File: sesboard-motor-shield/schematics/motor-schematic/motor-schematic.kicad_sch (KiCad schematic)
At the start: 0 parts

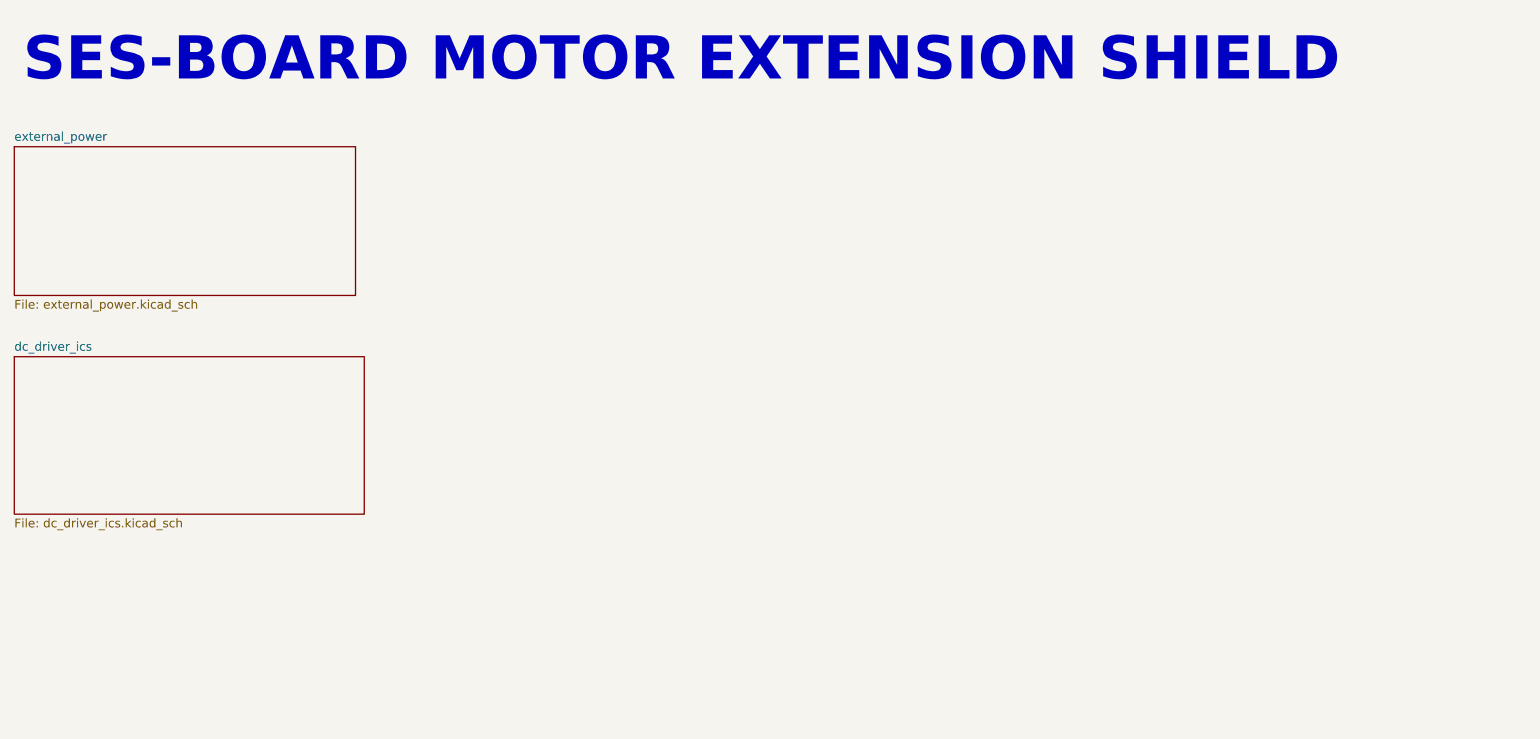
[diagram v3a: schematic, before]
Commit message: added global labels for motor drivers
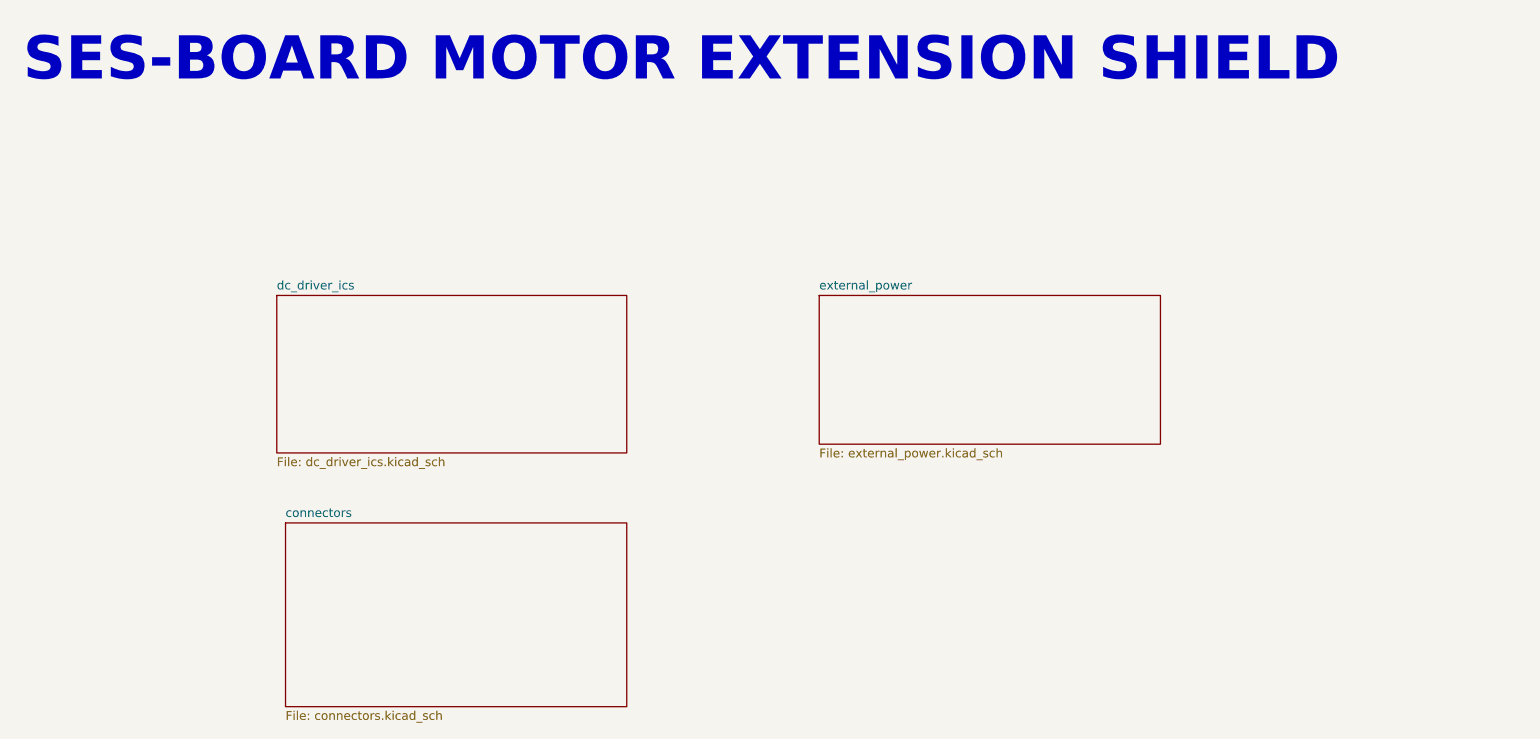
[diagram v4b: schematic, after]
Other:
- added sheet connectors (connectors.kicad_sch)
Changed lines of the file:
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@@
     (effects (font (size 6.27 6.27) (thickness 1.254) bold) (justify left bottom))
   )
-  (sheet (at 50.8 48.26) (size 49.53 21.59) (fields_autoplaced)
+  (sheet (at 90.17 102.87) (size 49.53 26.67) (fields_autoplaced)
     (stroke (width 0.1524) (type solid) (color 0 0 0 0))
     (fill (color 0 0 0 0.0000))
-    (property "Sheet name" "external_power" (id 0) (at 50.8 47.5484 0)
+    (property "Sheet name" "connectors" (id 0) (at 90.17 102.1584 0)
       (effects (font (size 1.27 1.27)) (justify left bottom))
     )
-    (property "Sheet file" "external_power.kicad_sch" (id 1) (at 50.8 70.4346 0)
+    (property "Sheet file" "connectors.kicad_sch" (id 1) (at 90.17 130.1246 0)
       (effects (font (size 1.27 1.27)) (justify left top))
     )
   )
-  (sheet (at 50.8 78.74) (size 50.8 22.86) (fields_autoplaced)
+  (sheet (at 167.64 69.85) (size 49.53 21.59) (fields_autoplaced)
     (stroke (width 0.1524) (type solid) (color 0 0 0 0))
     (fill (color 0 0 0 0.0000))
-    (property "Sheet name" "dc_driver_ics" (id 0) (at 50.8 78.0284 0)
+    (property "Sheet name" "external_power" (id 0) (at 167.64 69.1384 0)
       (effects (font (size 1.27 1.27)) (justify left bottom))
     )
-    (property "Sheet file" "dc_driver_ics.kicad_sch" (id 1) (at 50.8 102.1846 0)
+    (property "Sheet file" "external_power.kicad_sch" (id 1) (at 167.64 92.0246 0)
+      (effects (font (size 1.27 1.27)) (justify left top))
+    )
+  )
+  (sheet (at 88.9 69.85) (size 50.8 22.86) (fields_autoplaced)
+    (stroke (width 0.1524) (type solid) (color 0 0 0 0))
+    (fill (color 0 0 0 0.0000))
+    (property "Sheet name" "dc_driver_ics" (id 0) (at 88.9 69.1384 0)
+      (effects (font (size 1.27 1.27)) (justify left bottom))
+    )
+    (property "Sheet file" "dc_driver_ics.kicad_sch" (id 1) (at 88.9 93.2946 0)
       (effects (font (size 1.27 1.27)) (justify left top))
     )
@@
     (path "/93d2313f-0919-4c6f-b07d-ab630442d056" (page "2"))
     (path "/eeff06ce-5dd6-48ad-98cf-4489d7624b9c" (page "3"))
+    (path "/14cc8e54-6739-4c6f-a4bf-829f53e763f8" (page "4"))
   )
   (symbol_instances
@@
       (reference "#PWR025") (unit 1) (value "+5V") (footprint "")
     )
+    (path "/eeff06ce-5dd6-48ad-98cf-4489d7624b9c/d870bfca-195d-40b5-a5d5-c054209f3ecc"
+      (reference "#PWR?") (unit 1) (value "GND") (footprint "")
+    )
+    (path "/eeff06ce-5dd6-48ad-98cf-4489d7624b9c/e7b0b387-3fb1-41d8-b6b4-c4be9590eed9"
+      (reference "#PWR?") (unit 1) (value "GND") (footprint "")
+    )
     (path "/93d2313f-0919-4c6f-b07d-ab630442d056/d9ead9ee-c345-4017-a86b-e222369cda3f"
-      (reference "C1") (unit 1) (value "C") (footprint "")
+      (reference "C1") (unit 1) (value "C") (footprint "Capacitor_SMD:C_0603_1608Metric")
     )
     (path "/93d2313f-0919-4c6f-b07d-ab630442d056/5275729a-412a-4aea-939f-ed3f5e37f264"
-      (reference "C2") (unit 1) (value "10uF") (footprint "")
+      (reference "C2") (unit 1) (value "10uF") (footprint "Capacitor_SMD:C_0603_1608Metric")
     )
     (path "/93d2313f-0919-4c6f-b07d-ab630442d056/af78cc8e-1c8a-4ab5-9be6-d00d9f3661a8"
-      (reference "C3") (unit 1) (value "100nF") (footprint "")
+      (reference "C3") (unit 1) (value "100nF") (footprint "Capacitor_SMD:C_0603_1608Metric")
     )
     (path "/93d2313f-0919-4c6f-b07d-ab630442d056/2228ccfd-64fa-4f80-9e97-c17cd073ed77"
-      (reference "C4") (unit 1) (value "10uF") (footprint "")
+      (reference "C4") (unit 1) (value "10uF") (footprint "Capacitor_SMD:C_0603_1608Metric")
     )
     (path "/93d2313f-0919-4c6f-b07d-ab630442d056/22b8a583-4c69-4445-818a-792fb8c64310"
-      (reference "C5") (unit 1) (value "100nF") (footprint "")
+      (reference "C5") (unit 1) (value "100nF") (footprint "Capacitor_SMD:C_0603_1608Metric_Pad1.08x0.95mm_HandSolder")
     )
     (path "/93d2313f-0919-4c6f-b07d-ab630442d056/001a0253-6ecf-4292-a1f7-0f48edbbd35b"
-      (reference "D1") (unit 1) (value "GREEN_LED") (footprint "")
+      (reference "D1") (unit 1) (value "GREEN_LED") (footprint "LED_SMD:LED_0603_1608Metric")
     )
     (path "/93d2313f-0919-4c6f-b07d-ab630442d056/4f9418ba-9c6a-4f02-80b5-4d8b68173369"
-      (reference "J1") (unit 1) (value "Barrel_Jack") (footprint "")
+      (reference "J1") (unit 1) (value "Barrel_Jack") (footprint "Connector_BarrelJack:BarrelJack_Horizontal")
     )
     (path "/eeff06ce-5dd6-48ad-98cf-4489d7624b9c/c4453281-59ee-47d3-bd52-06aeb5935aac"
-      (reference "J2") (unit 1) (value "EXTERNAL_MOTOR_POWER") (footprint "")
+      (reference "J2") (unit 1) (value "EXTERNAL_MOTOR_POWER") (footprint "TerminalBlock_Phoenix:TerminalBlock_Phoenix_MKDS-1,5-2_1x02_P5.00mm_Horizontal")
     )
-    (path "/eeff06ce-5dd6-48ad-98cf-4489d7624b9c/d5013ac0-e1ec-465d-8ee5-8ced61108e8e"
-      (reference "J3") (unit 1) (value "MOTOR_C_OUT") (footprint "")
+    (path "/14cc8e54-6739-4c6f-a4bf-829f53e763f8/44d56e02-6f8b-4dba-a8f7-8cd6249ad3f6"
+      (reference "J3") (unit 1) (value "SESBOARD_1") (footprint "Connector_PinHeader_2.54mm:PinHeader_1x20_P2.54mm_Vertical")
     )
-    (path "/eeff06ce-5dd6-48ad-98cf-4489d7624b9c/bf4cd4e1-012f-42b7-8c27-76a7b81a4f28"
-      (reference "J4") (unit 1) (value "MOTOR_D_OUT") (footprint "")
+    (path "/14cc8e54-6739-4c6f-a4bf-829f53e763f8/19ccde18-a5b4-47c7-a5b9-970f62526c41"
+      (reference "J4") (unit 1) (value "SESBOARD_2") (footprint "Connector_PinHeader_2.54mm:PinHeader_1x20_P2.54mm_Vertical")
     )
-    (path "/eeff06ce-5dd6-48ad-98cf-4489d7624b9c/97dd2f34-1862-4f35-913e-e493c6a42577"
-      (reference "J5") (unit 1) (value "MOTOR_A_OUT") (footprint "")
+    (path "/eeff06ce-5dd6-48ad-98cf-4489d7624b9c/4c99bbb8-e08a-4485-a034-a4471d5dafb7"
+      (reference "J?") (unit 1) (value "MOTOR_C_OUT") (footprint "TerminalBlock_Phoenix:TerminalBlock_Phoenix_MKDS-1,5-2_1x02_P5.00mm_Horizontal")
     )
-    (path "/eeff06ce-5dd6-48ad-98cf-4489d7624b9c/46d2f3c8-d324-4c23-b645-72580d2b8836"
-      (reference "J6") (unit 1) (value "MOTOR_B_OUT") (footprint "")
+    (path "/eeff06ce-5dd6-48ad-98cf-4489d7624b9c/4e39e408-2fde-44c6-bac0-3fc3fd902fc3"
+      (reference "J?") (unit 1) (value "MOTOR_D_OUT") (footprint "TerminalBlock_Phoenix:TerminalBlock_Phoenix_MKDS-1,5-2_1x02_P5.00mm_Horizontal")
     )
-    (path "/eeff06ce-5dd6-48ad-98cf-4489d7624b9c/ef61c677-aa6b-4a16-87bd-bd33dcc48d96"
-      (reference "J7") (unit 1) (value "SERVO1") (footprint "")
+    (path "/eeff06ce-5dd6-48ad-98cf-4489d7624b9c/50f3c45b-3134-41b7-8c64-a49b87793127"
+      (reference "J?") (unit 1) (value "MOTOR_A_OUT") (footprint "TerminalBlock_Phoenix:TerminalBlock_Phoenix_MKDS-1,5-2_1x02_P5.00mm_Horizontal")
     )
-    (path "/eeff06ce-5dd6-48ad-98cf-4489d7624b9c/9a7af8e8-4c25-4519-9af0-ac5377662a39"
-      (reference "J8") (unit 1) (value "SERVO2") (footprint "")
+    (path "/eeff06ce-5dd6-48ad-98cf-4489d7624b9c/5420fce4-4014-4024-ac1c-89d0f8532d6f"
+      (reference "J?") (unit 1) (value "SERVO1") (footprint "Connector_PinHeader_2.54mm:PinHeader_1x03_P2.54mm_Vertical")
+    )
+    (path "/eeff06ce-5dd6-48ad-98cf-4489d7624b9c/ac52e3ff-c3dc-4f01-bf86-36c705c8e5cd"
+      (reference "J?") (unit 1) (value "MOTOR_B_OUT") (footprint "TerminalBlock_Phoenix:TerminalBlock_Phoenix_MKDS-1,5-2_1x02_P5.00mm_Horizontal")
+    )
+    (path "/eeff06ce-5dd6-48ad-98cf-4489d7624b9c/e672768b-ebf7-4766-93e5-85a3fb398f9b"
+      (reference "J?") (unit 1) (value "SERVO2") (footprint "Connector_PinHeader_2.54mm:PinHeader_1x03_P2.54mm_Vertical")
     )
     (path "/93d2313f-0919-4c6f-b07d-ab630442d056/ca07bcf5-811d-46aa-b849-0684aa3a6067"
-      (reference "Q1") (unit 1) (value "Q_NMOS_DGS") (footprint "")
+      (reference "Q1") (unit 1) (value "Q_NMOS_DGS") (footprint "Package_TO_SOT_THT:TO-220-3_Vertical")
     )
     (path "/93d2313f-0919-4c6f-b07d-ab630442d056/a6d7f9c6-9504-4931-812e-d87c7d38a45c"
@@
     )
     (path "/93d2313f-0919-4c6f-b07d-ab630442d056/e1d19d1a-90fd-4b02-851d-0f8a39066db3"
-      (reference "R1") (unit 1) (value "510") (footprint "")
+      (reference "R1") (unit 1) (value "510R") (footprint "Resistor_SMD:R_0603_1608Metric")
     )
     (path "/93d2313f-0919-4c6f-b07d-ab630442d056/06f09c2f-89c0-45c5-9ecb-66d7577cc34e"
-      (reference "R2") (unit 1) (value "510") (footprint "")
+      (reference "R2") (unit 1) (value "510R") (footprint "Resistor_SMD:R_0603_1608Metric")
     )
     (path "/93d2313f-0919-4c6f-b07d-ab630442d056/e1320052-63b8-4d04-a3b1-99858ebf302c"
-      (reference "RV1") (unit 1) (value "R_Potentiometer_Trim_US") (footprint "")
+      (reference "RV1") (unit 1) (value "R_Potentiometer_Trim_US") (footprint "Potentiometer_SMD:Potentiometer_Vishay_TS53YL_Vertical")
     )
     (path "/93d2313f-0919-4c6f-b07d-ab630442d056/ae0756d7-ed93-4874-bb3b-1e5d145ea0a5"
